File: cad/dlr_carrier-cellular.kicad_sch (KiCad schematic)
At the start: 13 parts, among them J6 U.FL, J7 SIM, U3 BG770A-NA, U4 TXS0108E

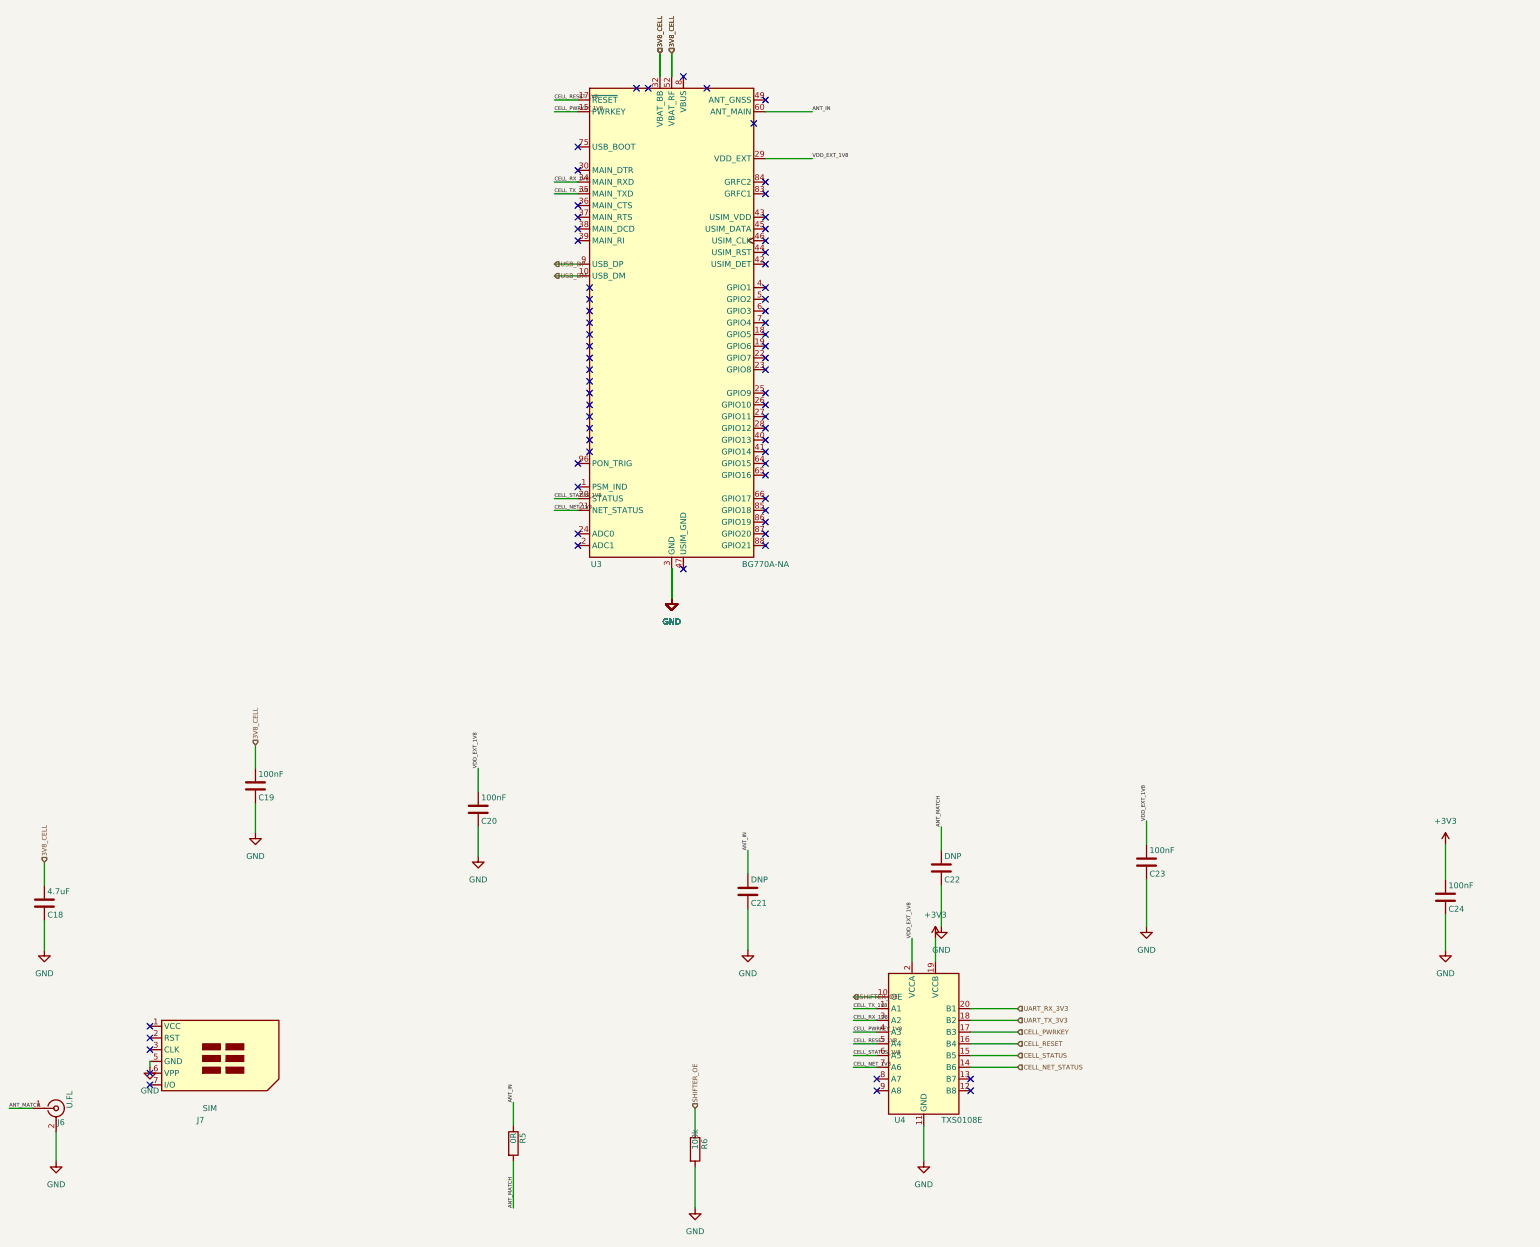
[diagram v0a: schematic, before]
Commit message: 🗺 feat(cad): scripted schematic + board pipeline, 4-layer stack
The committed board had almost every pad on +3V3 — no 5V_RAIL, VBAT or SDA1 net
existed on it at all — so the gerbers in output/ were never a valid board. Cause:
"Update PCB from Schematic" is GUI-only, so nothing kept the board honest, and the
schematic generator itself was merging nets.

Schematic generator:
  * power stubs now run along the pin direction; they used to be forced up or down
    regardless, which drove a 5V_RAIL stub straight through the buck inductor's
    BUCK_SW pin
  * PWR_FLAGs are placed by rule — any net that reaches a power-input pin with no
    power-output pin gets exactly one — instead of a hardcoded list, which is what
    the new VBAT and CHG_VCC rails needed
  * placement is deterministic; it used Python's salted hash(), so no two runs
    produced the same schematic
  * sch_guard fails the build on any cross-net wire/pin collision
  * ~700 lines of dead single-sheet generator removed
  ERC: 0 violations across all 8 sheets.

Board pipeline (cad/drawing/, all scripted, no GUI step):
  sync_pcb      rebuilds every footprint from the library and reassigns every pad
                net from the SKiDL netlist — the replacement for F8
  board_setup   4-layer SIG/GND/5V/SIG stack, rules, net classes, planes (ADR-016)
  route_pcb     DSN -> Freerouting -> SES, after patching the DSN so plane layers
                are "power" (the router was slicing the planes with signals) and
                the plane declarations are dropped (the router had been leaving
                GND and 5V pads with no path to the plane at all)
  stitch_planes vias from surface pads into their plane
  close_gaps    closes what the router leaves, using real segment-to-segment
                clearance; it never forces copper through another net

DRC: 265 unconnected -> 5, with no clearance, short, annular-ring or courtyard
errors. The remaining 5 are escapes on the DF40, the VQFN and the MSOP; they are
l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
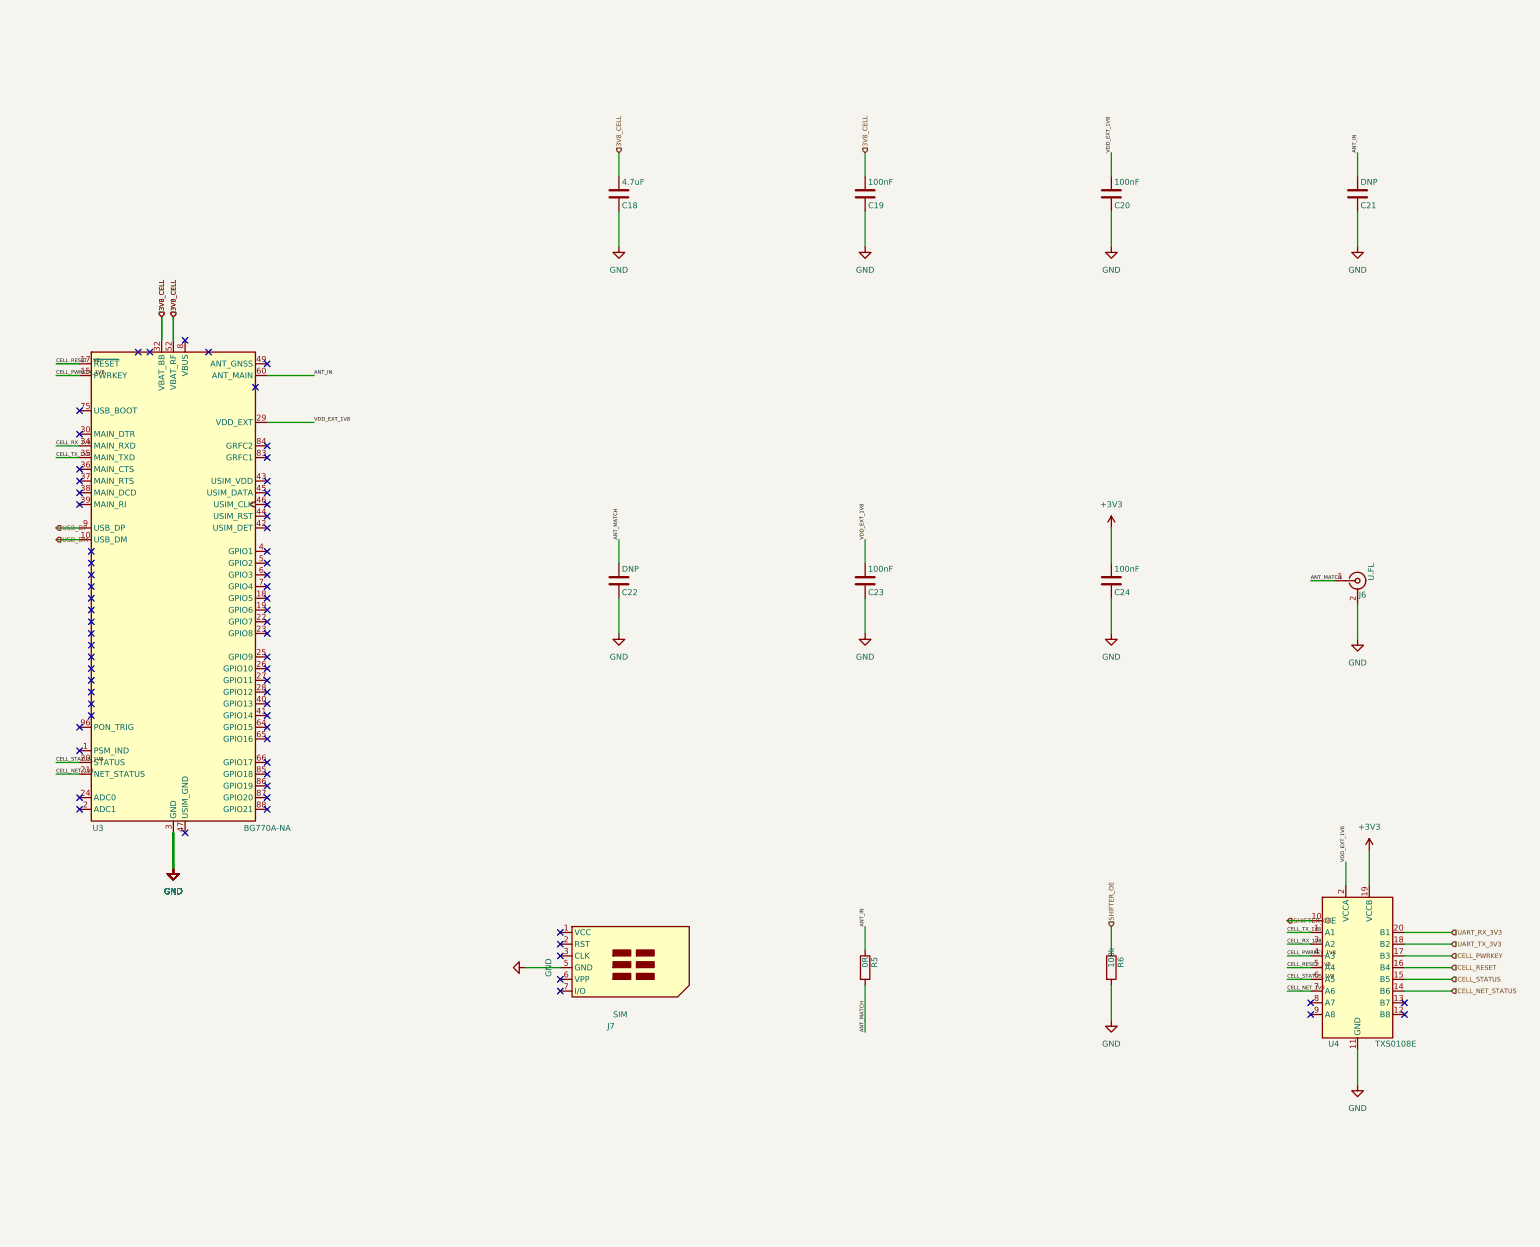
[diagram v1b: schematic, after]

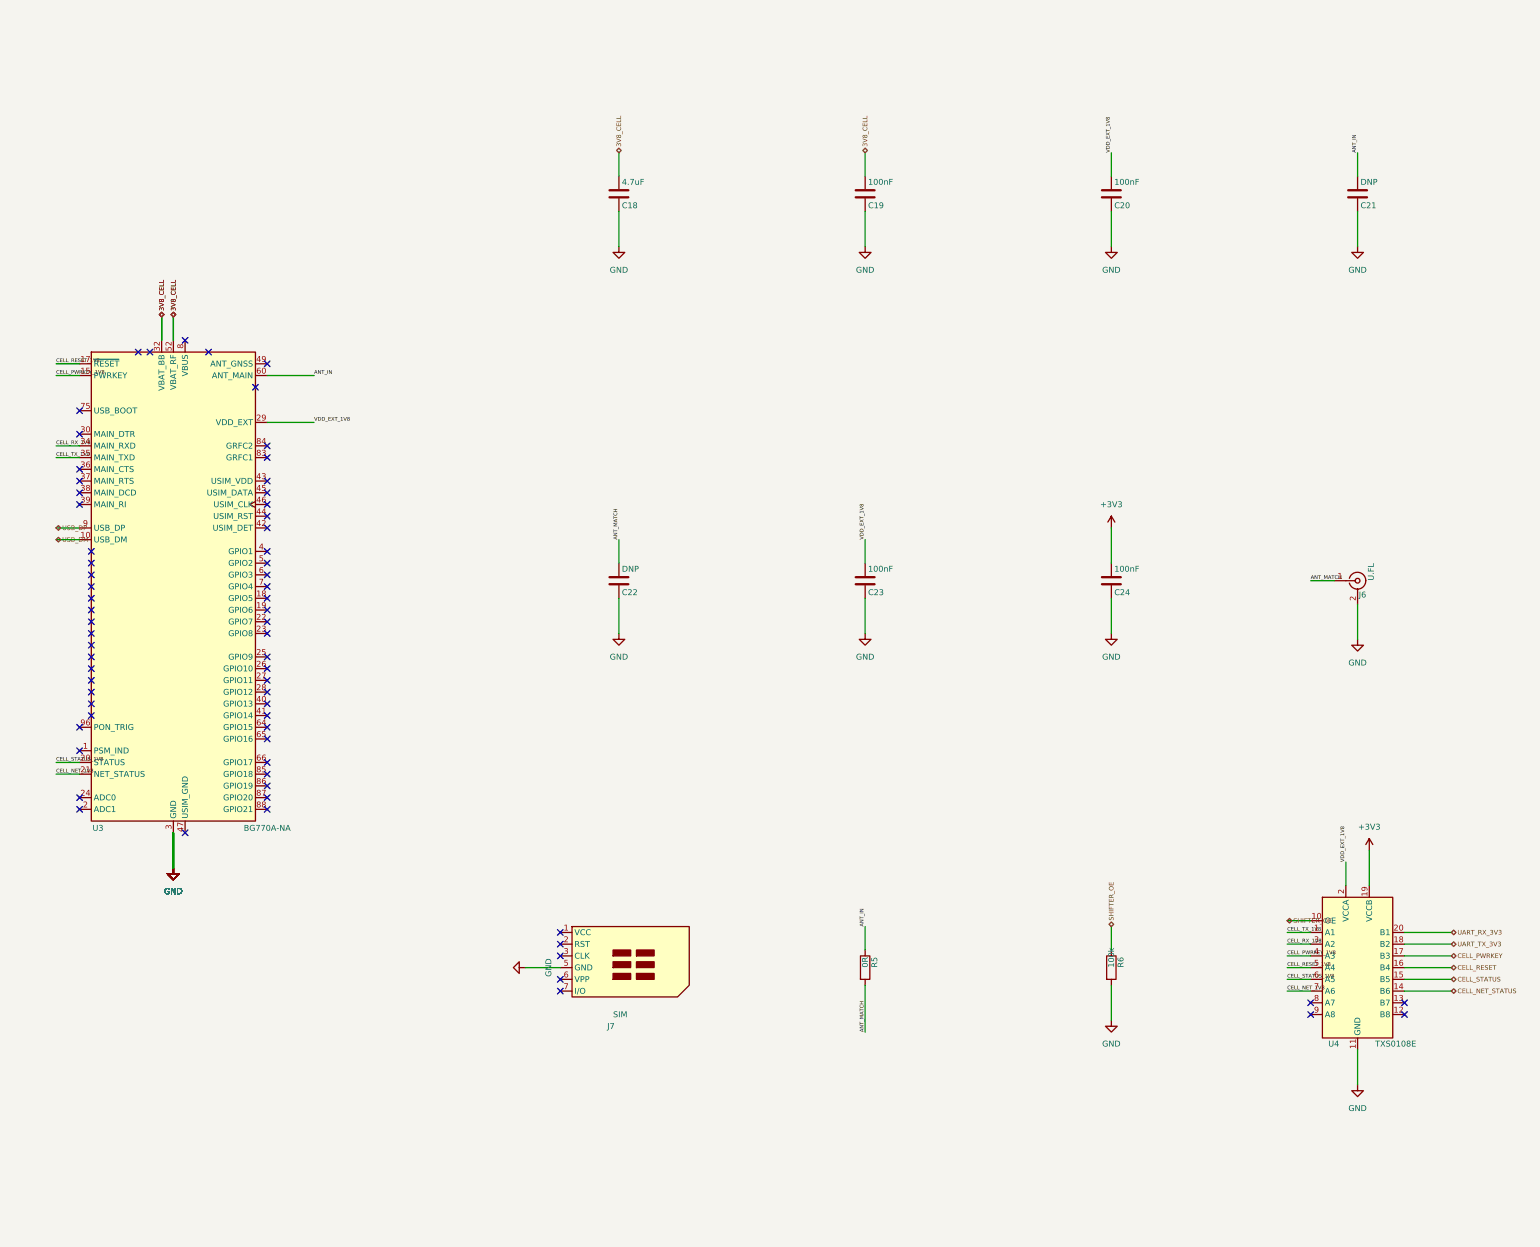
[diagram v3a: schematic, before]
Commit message: 🩺 refactor(schematic): cross-sheet nets via global labels, no sheet pins
Three attempts at making the hierarchical sheet-pin mechanism pass KiCad 9 failed
(project name, instance paths, label type), so the mechanism goes. Cross-sheet nets
now connect by name through global labels on the child sheets; the root carries
sheet symbols only — no pins, no stub wires, no labels.

That removes the whole hier_label_mismatch / label_dangling class rather than
chasing it, and it matches the connectivity style the generate-schematic skill
already prescribes for this project ("all inter-block connections use net labels").

kicad-sch-api's add_global_label still does not serialize, so the labels are emitted
as hierarchical and rewritten in the saved sheet.

Co-Authored-By: Claude Opus 5 <noreply@anthropic.com>
Claude-Session: https://claude.ai/code/session_011xr7VCL7rkJj2WE2uQF7sF
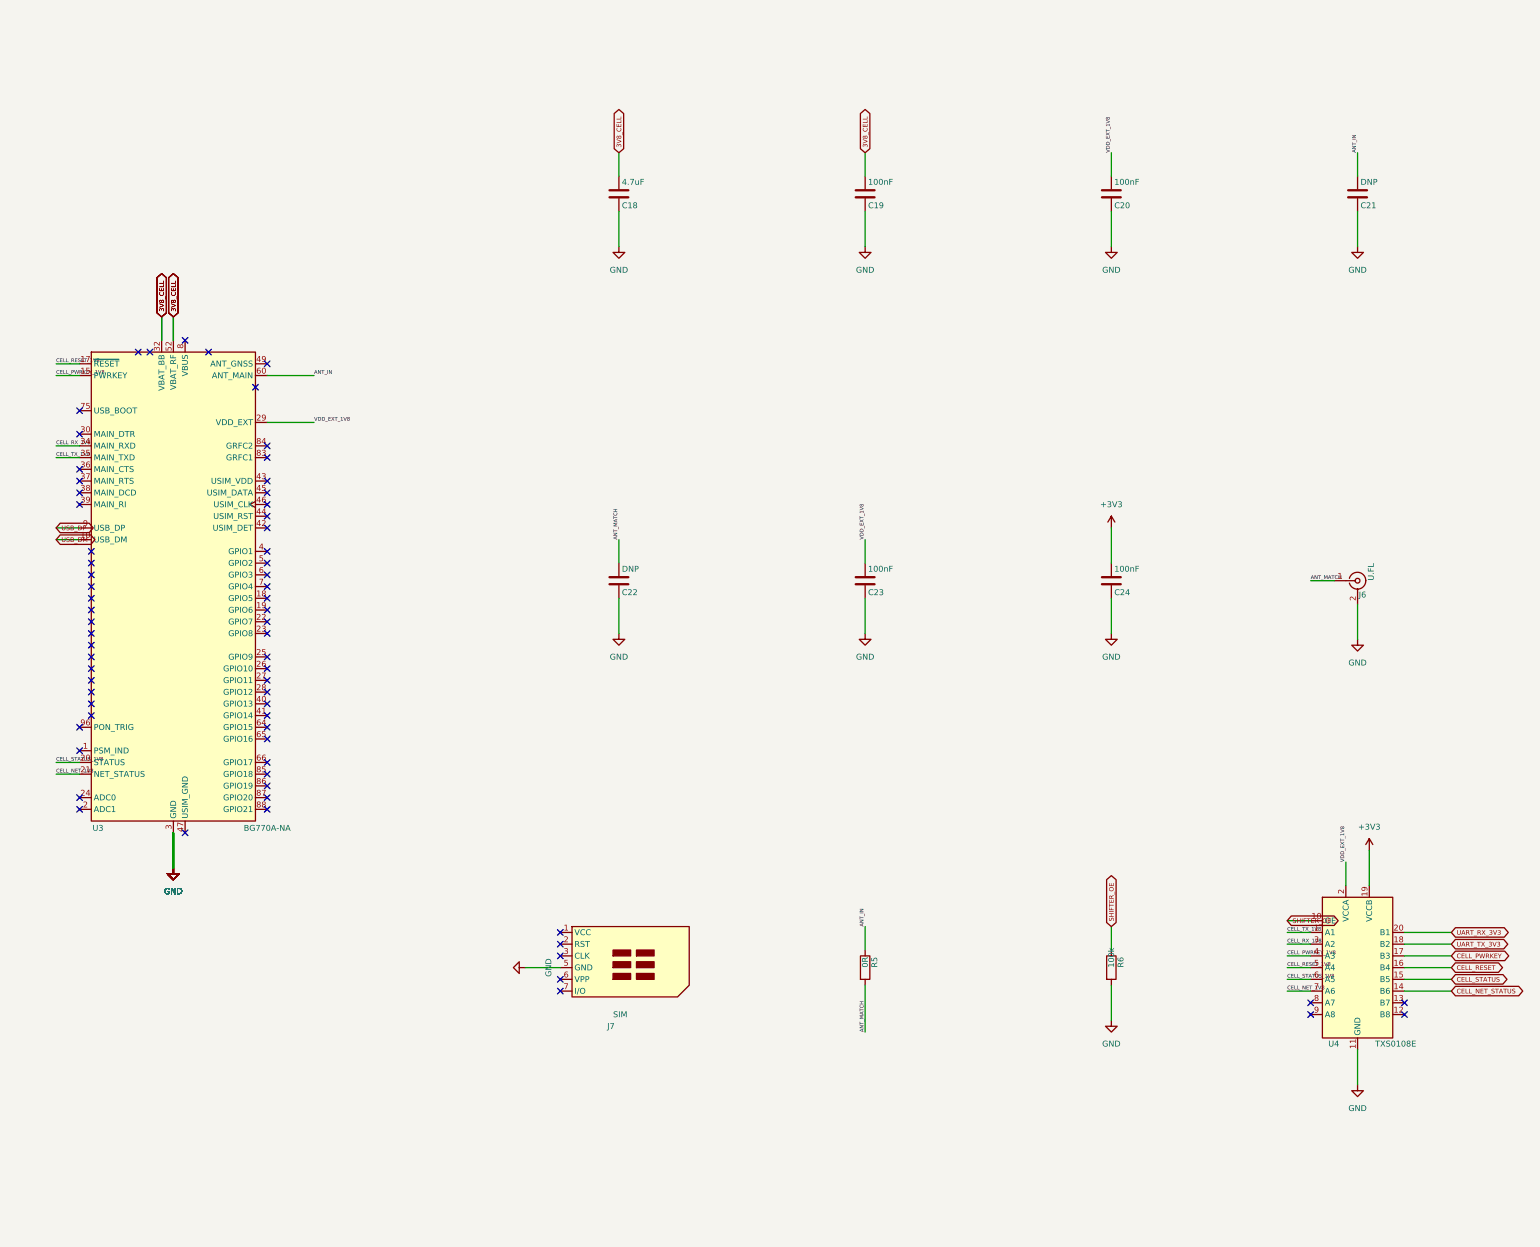
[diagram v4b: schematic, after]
